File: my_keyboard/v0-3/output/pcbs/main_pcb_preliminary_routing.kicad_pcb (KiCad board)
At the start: 2 copper layers, 136.8 x 106.8 mm, 27 parts

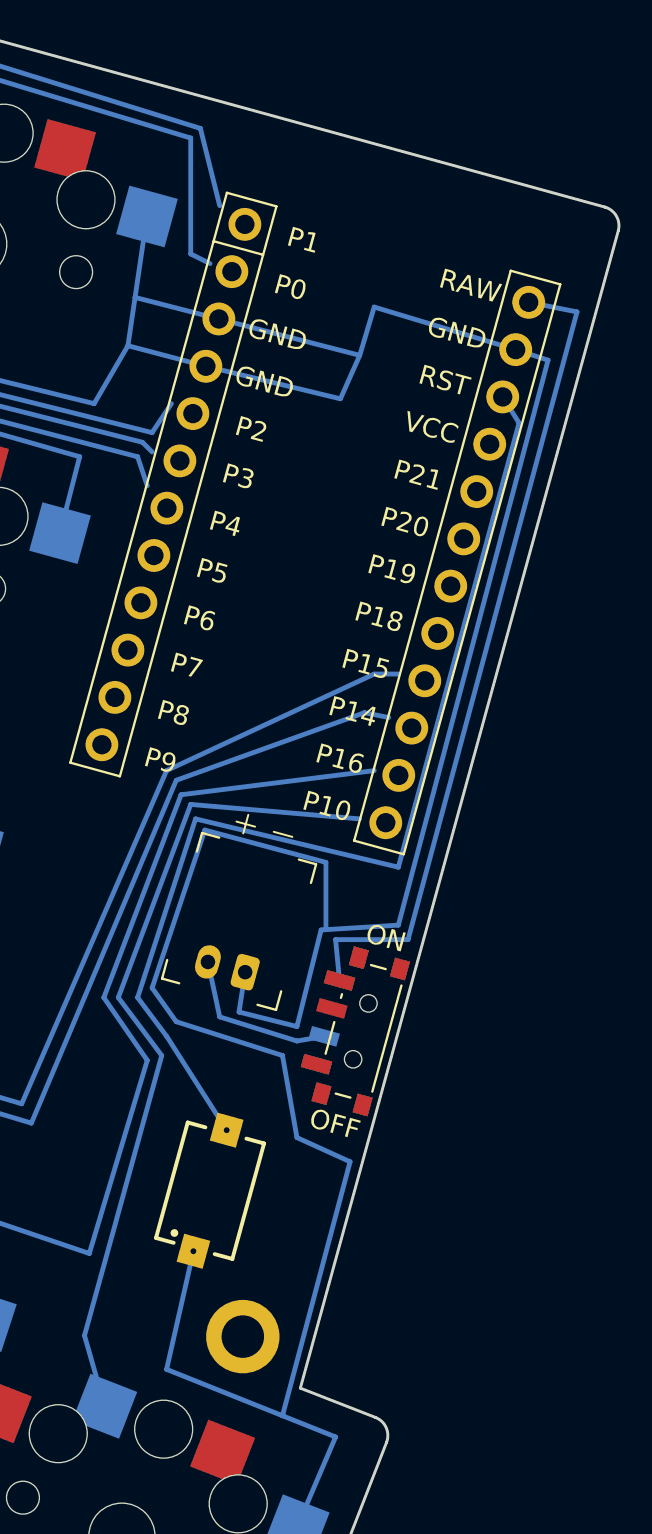
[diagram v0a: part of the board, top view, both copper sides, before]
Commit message: Add docs and v0-3
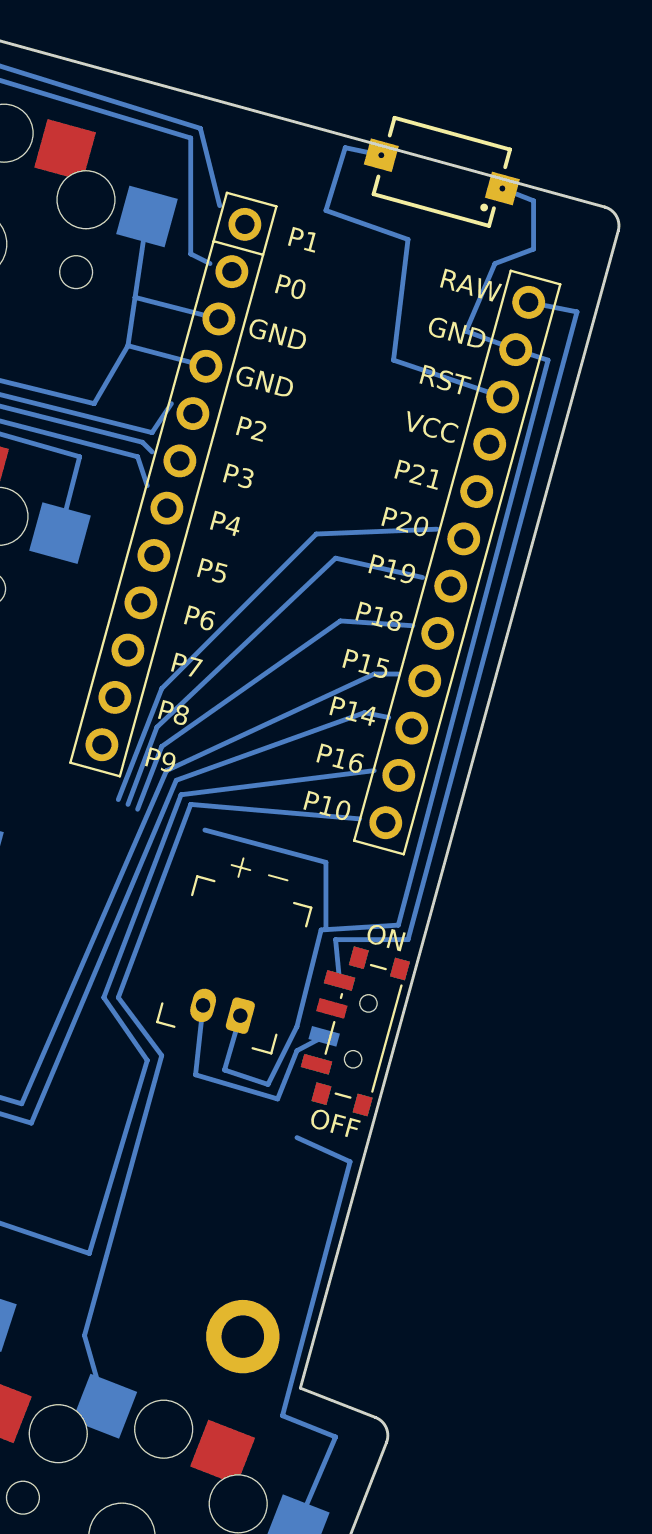
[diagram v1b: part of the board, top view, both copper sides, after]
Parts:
- moved S18 54.1 mm to (187.0, 45.2), turned to 164.64 degrees
- moved JST1 2.26 mm to (175.6, 88.7)
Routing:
- net (no net): track 0.00 -> 63.9 mm
- net GND: track 813.9 -> 769.3 mm
- net RST: track 54.2 -> 22.1 mm
- net PWR_SW: track 8.53 -> 12.3 mm
